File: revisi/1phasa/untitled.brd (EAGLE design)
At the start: 80 x 102 mm, 52 parts, among them J1 U.FL-R-SMT(01), J2 10118193-0001LF, K1 SLA-05VDC-SL-C, Q1 S9013, Q16 MMBT3904, Q17 MMBT3904, Q18 12MHz, U1 AMS1117, U19 CH340G, U2 PC817X2NIP0F, U3 ESP32-WROOM-32D

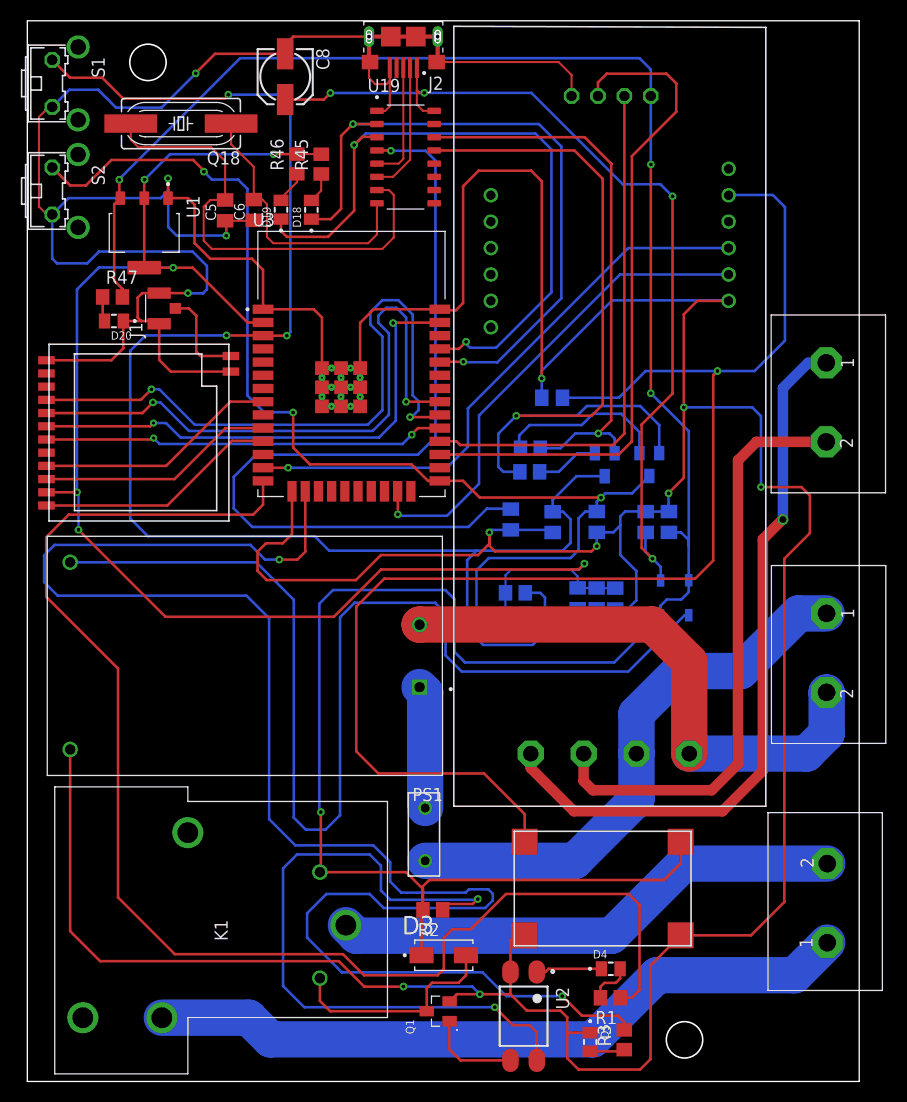
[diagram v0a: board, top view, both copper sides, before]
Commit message: revisi firmware tentang jumlah lampu
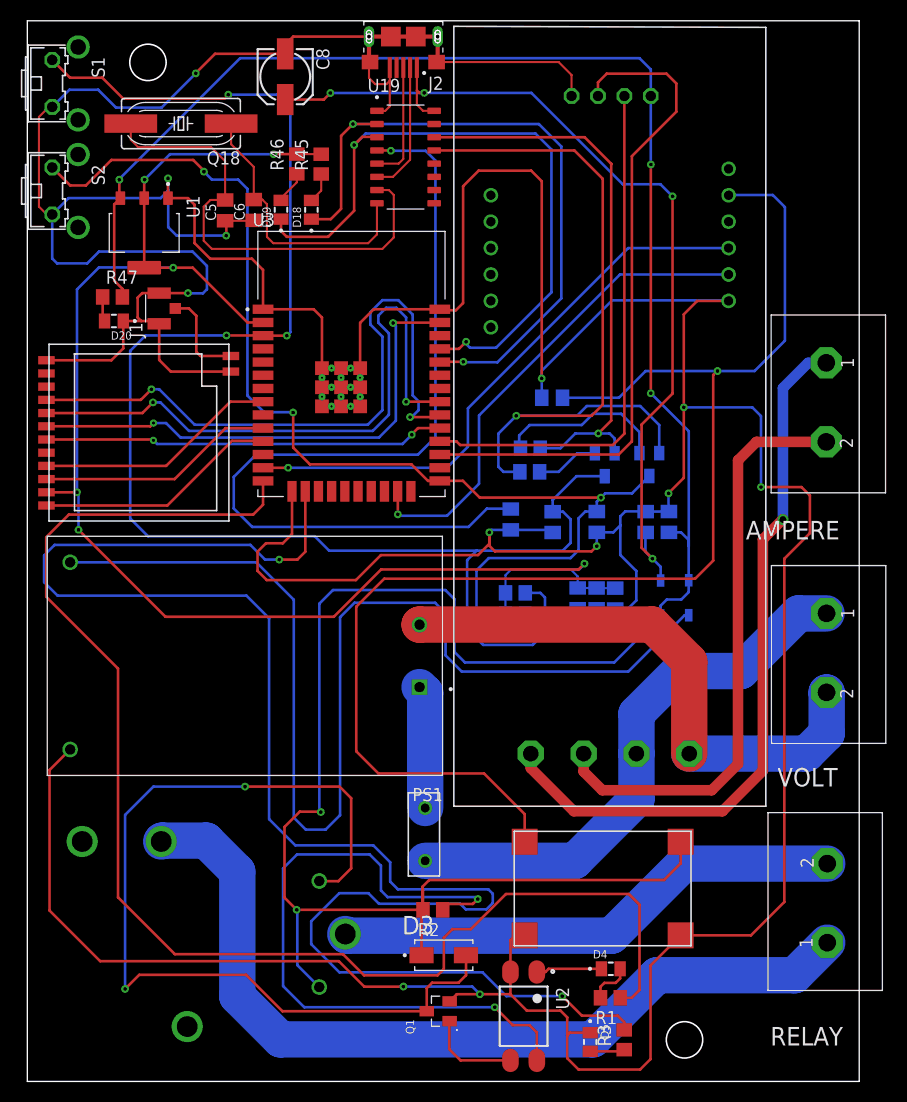
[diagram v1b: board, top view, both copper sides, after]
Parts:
- moved K1 0.85 mm to (30.6, 3.18), flipped to the bottom, turned to 270 degrees
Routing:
- net N$7: track 21.3 -> 89.9 mm, vias 0 -> 2
- net VCC: track 241.5 -> 258.2 mm, vias 4 -> 5
- net N$19: track 68.7 -> 82.9 mm
- net GND: track 576.9 -> 578.5 mm
- net LED-LORA: track 160.1 -> 159.3 mm
- net N$17: track 57.3 -> 56.8 mm
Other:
- board text added: "AMPERE"
- board text added: "RELAY"
- board text added: "VOLT"

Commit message: fix
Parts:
- R2, R3, R47: value 10k -> 1k
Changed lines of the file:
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@@
 <attribute name="VALUE" x="56.706540625" y="-0.418321875" size="1.27" layer="27" rot="R180"/>
 </element>
-<element name="R2" library="rcl" library_urn="urn:adsk.eagle:library:334" package="R0805" package3d_urn="urn:adsk.eagle:package:23553/2" value="10k" x="38.997128125" y="5.505603125" smashed="yes" rot="R180">
+<element name="R2" library="rcl" library_urn="urn:adsk.eagle:library:334" package="R0805" package3d_urn="urn:adsk.eagle:package:23553/2" value="1k" x="38.997128125" y="5.505603125" smashed="yes" rot="R180">
 <attribute name="NAME" x="39.632128125" y="4.235603125" size="1.27" layer="25" rot="R180"/>
 <attribute name="POPULARITY" value="86" x="-0.372871875" y="107.105603125" size="1.778" layer="27" rot="R180" display="off"/>
@@
 <attribute name="VALUE" x="28.455390625" y="76.59524375" size="1.27" layer="27" rot="R90"/>
 </element>
-<element name="R47" library="rcl" library_urn="urn:adsk.eagle:library:334" package="R0805" package3d_urn="urn:adsk.eagle:package:23553/2" value="10k" x="8.194" y="64.442871875" smashed="yes">
+<element name="R47" library="rcl" library_urn="urn:adsk.eagle:library:334" package="R0805" package3d_urn="urn:adsk.eagle:package:23553/2" value="1k" x="8.194" y="64.442871875" smashed="yes">
 <attribute name="NAME" x="7.559" y="65.712871875" size="1.27" layer="25"/>
 <attribute name="POPULARITY" value="86" x="37.404" y="-37.157128125" size="1.778" layer="27" display="off"/>
@@
 <attribute name="MF" value="Sharp Microelectronics" x="-36.09193125" y="-28.854778125" size="1.778" layer="27" rot="R270" display="off"/>
 <attribute name="MP" value="PC817X2NIP0F" x="-36.09193125" y="-28.854778125" size="1.778" layer="27" rot="R270" display="off"/>
+<attribute name="NAME" x="50.83386875" y="-1.9195375" size="1.27238125" layer="25" rot="R270"/>
 <attribute name="NAME" x="50.8300875" y="-1.922946875" size="1.27083125" layer="25" rot="R270"/>
-<attribute name="NAME" x="50.83386875" y="-1.9195375" size="1.27238125" layer="25" rot="R270"/>
 <attribute name="PACKAGE" value="SMD-4 Sharp Microelectronics" x="-36.09193125" y="-28.854778125" size="1.778" layer="27" rot="R270" display="off"/>
 <attribute name="PRICE" value="None" x="-36.09193125" y="-28.854778125" size="1.778" layer="27" rot="R270" display="off"/>
@@
 <attribute name="PURCHASE-URL" value="https://pricing.snapeda.com/search/part/SML-LXT0805IW-TR/?ref=eda" x="54.130403125" y="-7.20664375" size="1.778" layer="27" rot="R270" display="off"/>
 </element>
-<element name="R3" library="rcl" library_urn="urn:adsk.eagle:library:334" package="R0805" package3d_urn="urn:adsk.eagle:package:23553/2" value="10k" x="57.40076875" y="-6.994178125" smashed="yes" rot="R90">
+<element name="R3" library="rcl" library_urn="urn:adsk.eagle:library:334" package="R0805" package3d_urn="urn:adsk.eagle:package:23553/2" value="1k" x="57.40076875" y="-6.994178125" smashed="yes" rot="R90">
 <attribute name="NAME" x="56.13076875" y="-7.629178125" size="1.27" layer="25" rot="R90"/>
 <attribute name="POPULARITY" value="86" x="57.40076875" y="-6.994178125" size="1.778" layer="27" rot="R90" display="off"/>
